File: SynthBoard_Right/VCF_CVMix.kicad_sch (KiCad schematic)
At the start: 21 parts, among them IC1 AS321KTR-G1, Q3 2SA812, Q4 2SC1623(RANGE:300-400), Q7 2SA812

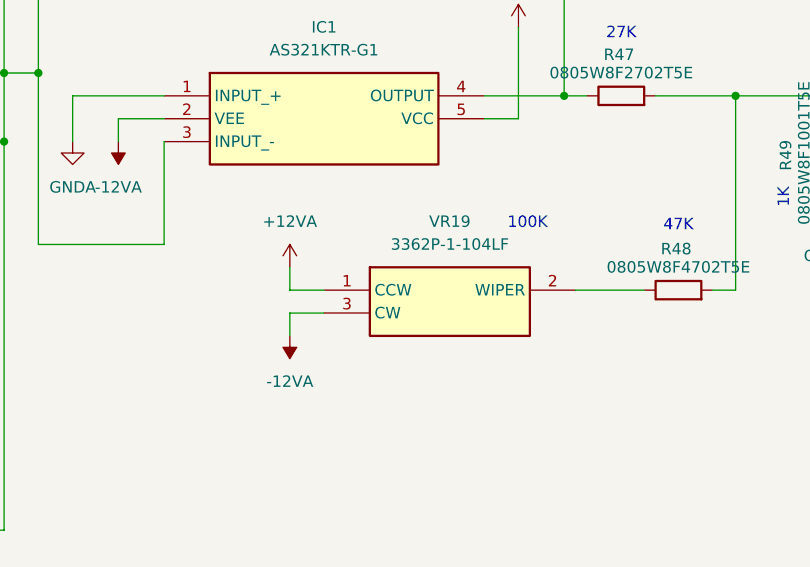
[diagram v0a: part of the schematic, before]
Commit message: SynthBoard Right
配線ミスを修正
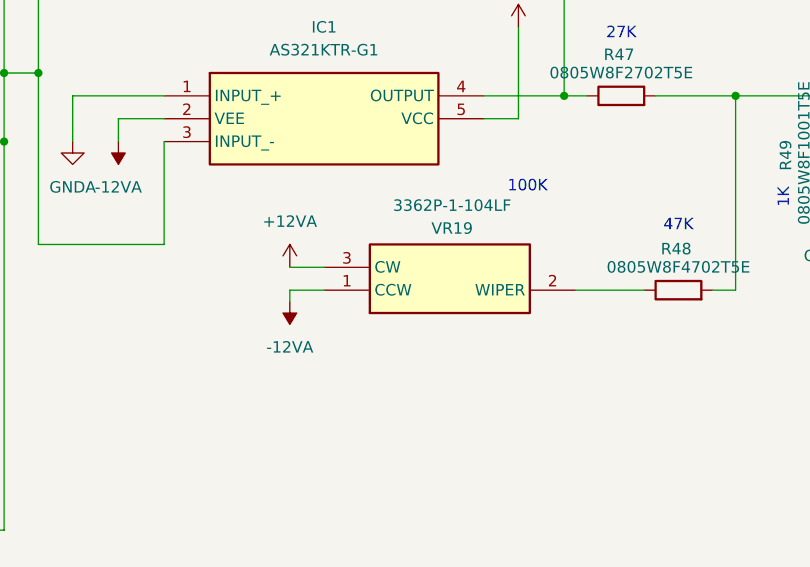
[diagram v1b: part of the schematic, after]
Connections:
- net +12VA: now also VR19.3 (CW); no longer VR19.1 (CCW)
- net -12VA: now also VR19.1 (CCW); no longer VR19.3 (CW)
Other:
- moved on the sheet: VR19
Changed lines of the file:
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@@
 	(text "100K"
 		(exclude_from_sim no)
-		(at 176.276 98.044 0)
+		(at 176.276 93.98 0)
 		(effects
 			(font
@@
 	(wire
 		(pts
-			(xy 153.67 105.41) (xy 149.86 105.41)
-		)
-		(stroke
-			(width 0)
-			(type default)
-		)
-	)
-	(wire
-		(pts
 			(xy 226.06 99.06) (xy 226.06 104.14)
 		)
@@
 	(wire
 		(pts
-			(xy 149.86 105.41) (xy 149.86 102.87)
+			(xy 66.04 121.92) (xy 68.58 121.92)
 		)
 		(stroke
@@
 	(wire
 		(pts
-			(xy 66.04 121.92) (xy 68.58 121.92)
+			(xy 81.28 16.51) (xy 81.28 20.32)
 		)
 		(stroke
@@
 	(wire
 		(pts
-			(xy 81.28 16.51) (xy 81.28 20.32)
+			(xy 85.09 140.97) (xy 85.09 147.32)
 		)
 		(stroke
@@
 	(wire
 		(pts
-			(xy 85.09 140.97) (xy 85.09 147.32)
+			(xy 121.92 100.33) (xy 121.92 81.28)
 		)
 		(stroke
@@
 	(wire
 		(pts
-			(xy 121.92 100.33) (xy 121.92 81.28)
+			(xy 135.89 83.82) (xy 125.73 83.82)
 		)
 		(stroke
@@
 	(wire
 		(pts
-			(xy 135.89 83.82) (xy 125.73 83.82)
+			(xy 149.86 102.87) (xy 153.67 102.87)
 		)
 		(stroke
@@
 	(wire
 		(pts
-			(xy 149.86 107.95) (xy 149.86 110.49)
-		)
-		(stroke
-			(width 0)
-			(type default)
-		)
-	)
-	(wire
-		(pts
 			(xy 125.73 83.82) (xy 125.73 88.9)
 		)
@@
 	(wire
 		(pts
-			(xy 153.67 107.95) (xy 149.86 107.95)
+			(xy 31.75 16.51) (xy 39.37 16.51)
 		)
 		(stroke
@@
 	(wire
 		(pts
-			(xy 31.75 16.51) (xy 39.37 16.51)
+			(xy 240.03 99.06) (xy 240.03 91.44)
 		)
 		(stroke
@@
 	(wire
 		(pts
-			(xy 240.03 99.06) (xy 240.03 91.44)
+			(xy 66.04 160.02) (xy 66.04 162.56)
 		)
 		(stroke
@@
 	(wire
 		(pts
-			(xy 66.04 160.02) (xy 66.04 162.56)
+			(xy 80.01 67.31) (xy 82.55 67.31)
 		)
 		(stroke
@@
 	(wire
 		(pts
-			(xy 80.01 67.31) (xy 82.55 67.31)
+			(xy 68.58 160.02) (xy 68.58 158.75)
 		)
 		(stroke
@@
 	(wire
 		(pts
-			(xy 68.58 160.02) (xy 68.58 158.75)
+			(xy 149.86 105.41) (xy 149.86 106.68)
 		)
 		(stroke
@@
 	(wire
 		(pts
+			(xy 153.67 105.41) (xy 149.86 105.41)
+		)
+		(stroke
+			(width 0)
+			(type default)
+		)
+	)
+	(wire
+		(pts
 			(xy 135.89 88.9) (xy 135.89 100.33)
 		)
@@
 	(symbol
 		(lib_id "power:-12VA")
-		(at 149.86 110.49 180)
+		(at 149.86 106.68 180)
 		(unit 1)
 		(exclude_from_sim no)
@@
 		(fields_autoplaced yes)
 		(property "Reference" "#PWR049"
-			(at 149.86 106.68 0)
+			(at 149.86 102.87 0)
 			(effects
 				(font
@@
 		)
 		(property "Value" "-12VA"
-			(at 149.86 115.57 0)
+			(at 149.86 111.76 0)
 			(effects
 				(font
@@
 		)
 		(property "Footprint" ""
-			(at 149.86 110.49 0)
+			(at 149.86 106.68 0)
 			(effects
 				(font
@@
 		)
 		(property "Datasheet" ""
-			(at 149.86 110.49 0)
+			(at 149.86 106.68 0)
 			(effects
 				(font
@@
 		)
 		(property "Description" "Power symbol creates a global label with name \"-12VA\""
-			(at 149.86 110.49 0)
+			(at 149.86 106.68 0)
 			(effects
 				(font
@@
 		(lib_id "SamacSys_Parts:3362P-1-103LF")
 		(at 153.67 105.41 0)
+		(mirror x)
 		(unit 1)
 		(exclude_from_sim no)
@@
 		(on_board yes)
 		(dnp no)
-		(fields_autoplaced yes)
 		(property "Reference" "VR19"
-			(at 167.64 97.79 0)
+			(at 167.894 98.552 0)
 			(effects
 				(font
@@
 		)
 		(property "Value" "3362P-1-104LF"
-			(at 167.64 100.33 0)
+			(at 167.894 96.012 0)
 			(effects
 				(font
@@
 		)
 		(property "Footprint" "SamacSys_parts:3362P_1"
-			(at 177.8 200.33 0)
+			(at 177.8 10.49 0)
 			(effects
 				(font
@@
 		)
 		(property "Datasheet" "https://datasheet.datasheetarchive.com/originals/distributors/SFDatasheet-6/sf-000139931.pdf"
-			(at 177.8 300.33 0)
+			(at 177.8 -89.51 0)
 			(effects
 				(font
@@
 		)
 		(property "Height" ""
-			(at 177.8 500.33 0)
+			(at 177.8 -289.51 0)
 			(effects
 				(font
@@
 		)
 		(property "Manufacturer_Name" "Bourns"
-			(at 177.8 600.33 0)
+			(at 177.8 -389.51 0)
 			(effects
 				(font
@@
 		)
 		(property "Manufacturer_Part_Number" "3362P-1-103LF"
-			(at 177.8 700.33 0)
+			(at 177.8 -489.51 0)
 			(effects
 				(font
@@
 		)
 		(property "Mouser Part Number" "652-3362P-1-103LF"
-			(at 177.8 800.33 0)
+			(at 177.8 -589.51 0)
 			(effects
 				(font
@@
 		)
 		(property "Mouser Price/Stock" "https://www.mouser.co.uk/ProductDetail/Bourns/3362P-1-103LF?qs=tS7CBNq%252BQ07BavGNEQud%252BA%3D%3D"
-			(at 177.8 900.33 0)
+			(at 177.8 -689.51 0)
 			(effects
 				(font
@@
 		)
 		(property "Arrow Part Number" "3362P-1-103LF"
-			(at 177.8 1000.33 0)
+			(at 177.8 -789.51 0)
 			(effects
 				(font
@@
 		)
 		(property "Arrow Price/Stock" "https://www.arrow.com/en/products/3362p-1-103lf/bourns?utm_currency=USD&region=nac"
-			(at 177.8 1100.33 0)
+			(at 177.8 -889.51 0)
 			(effects
 				(font

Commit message: SynthBoard Right
Basic部品で更新まで
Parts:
- removed Q4: 2SC1623(RANGE:300-400), SamacSys_parts:SOT95P237X125-3N, symbol SamacSys_Parts:2SC1623-A
- added Q1: SS8050(RANGE:200-350), Package_TO_SOT_SMD:SOT-23, symbol Transistor_BJT:SS8050
- R50: value 0805W8J0104T5E -> 0805W8F1003T5E
- renumbered Q3 to Q4
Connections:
- net +12VA: now also Q1.3 (C)
- net at R47.2, R48.2, R49.2: now also Q1.1 (B)
- net at Q4.1 (B), R50.2: now also Q1.2 (E)
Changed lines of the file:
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@@
 	(wire
 		(pts
-			(xy 226.06 91.44) (xy 226.06 99.06)
-		)
-		(stroke
-			(width 0)
-			(type default)
-		)
-	)
-	(wire
-		(pts
-			(xy 209.55 83.82) (xy 215.9 83.82)
+			(xy 209.55 83.82) (xy 218.44 83.82)
 		)
 		(stroke
@@
 	(wire
 		(pts
+			(xy 226.06 76.2) (xy 226.06 78.74)
+		)
+		(stroke
+			(width 0)
+			(type default)
+		)
+	)
+	(wire
+		(pts
 			(xy 196.85 105.41) (xy 199.39 105.41)
 		)
@@
 	(wire
 		(pts
+			(xy 226.06 88.9) (xy 226.06 99.06)
+		)
+		(stroke
+			(width 0)
+			(type default)
+		)
+	)
+	(wire
+		(pts
 			(xy 31.75 16.51) (xy 39.37 16.51)
 		)
@@
 		(on_board yes)
 		(dnp no)
-		(property "Reference" "Q3"
+		(property "Reference" "Q4"
 			(at 261.62 90.1699 0)
 			(effects
@@
 			(project "SynthBoard"
 				(path "/92765e2f-a998-485f-b610-76a9d5b50cba/91d0d04c-ea81-4181-b7cc-4c199a791c3e"
-					(reference "Q3")
+					(reference "Q4")
 					(unit 1)
 				)
@@
 			)
 		)
-		(property "Value" "0805W8J0104T5E"
+		(property "Value" "0805W8F1003T5E"
 			(at 223.52 107.95 90)
 			(effects
@@
 	)
 	(symbol
+		(lib_id "Transistor_BJT:SS8050")
+		(at 223.52 83.82 0)
+		(unit 1)
+		(exclude_from_sim no)
+		(in_bom yes)
+		(on_board yes)
+		(dnp no)
+		(fields_autoplaced yes)
+		(property "Reference" "Q1"
+			(at 228.6 82.5499 0)
+			(effects
+				(font
+					(size 1.27 1.27)
+				)
+				(justify left)
+			)
+		)
+		(property "Value" "SS8050(RANGE:200-350)"
+			(at 228.6 85.0899 0)
+			(effects
+				(font
+					(size 1.27 1.27)
+				)
+				(justify left)
+			)
+		)
+		(property "Footprint" "Package_TO_SOT_SMD:SOT-23"
+			(at 228.6 91.186 0)
+			(effects
+				(font
+					(size 1.27 1.27)
+					(italic yes)
+				)
+				(justify left)
+				(hide yes)
+			)
+		)
+		(property "Datasheet" "http://www.secosgmbh.com/datasheet/products/SSMPTransistor/SOT-23/SS8050.pdf"
+			(at 228.6 88.646 0)
+			(effects
+				(font
+					(size 1.27 1.27)
+				)
+				(justify left)
+				(hide yes)
+			)
+		)
+		(property "Description" "General Purpose NPN Transistor, 1.5A Ic, 25V Vce, SOT-23"
+			(at 257.556 86.106 0)
+			(effects
+				(font
+					(size 1.27 1.27)
+				)
+				(hide yes)
+			)
+		)
+		(pin "2"
+		)
+		(pin "3"
+		)
+		(pin "1"
+		)
+		(instances
+			(project ""
+				(path "/92765e2f-a998-485f-b610-76a9d5b50cba/91d0d04c-ea81-4181-b7cc-4c199a791c3e"
+					(reference "Q1")
+					(unit 1)
+				)
+			)
+		)
+	)
+	(symbol
 		(lib_id "SamacSys_Parts:AS321KTR-E1")
 		(at 135.89 83.82 0)
@@
 					(unit 1)
 				)
-			)
-		)
-	)
-	(symbol
-		(lib_id "SamacSys_Parts:2SC1623-A")
-		(at 215.9 83.82 0)
-		(unit 1)
-		(exclude_from_sim no)
-		(in_bom yes)
-		(on_board yes)
-		(dnp no)
-		(fields_autoplaced yes)
-		(property "Reference" "Q4"
-			(at 229.87 82.5499 0)
-			(effects
-				(font
-					(size 1.27 1.27)
-				)
-				(justify left)
-			)
-		)
-		(property "Value" "2SC1623(RANGE:300-400)"
-			(at 229.87 85.0899 0)
-			(effects
-				(font
-					(size 1.27 1.27)
-				)
-				(justify left)
-			)
-		)
-		(property "Footprint" "SamacSys_parts:SOT95P237X125-3N"
-			(at 229.87 185.09 0)
-			(effects
-				(font
-					(size 1.27 1.27)
-				)
-				(justify left top)
-				(hide yes)
-			)
-		)
-		(property "Datasheet" "https://www.mouser.in/datasheet/2/258/2SC1623_SOT_23_-1625845.pdf"
-			(at 229.87 285.09 0)
-			(effects
-				(font
-					(size 1.27 1.27)
-				)
-				(justify left top)
-				(hide yes)
-			)
-		)
-		(property "Description" "Renesas Electronics 2SC1623-A NPN Bipolar Transistor, 100 mA, 50 V, 3-Pin MiniMold"
-			(at 215.9 83.82 0)
-			(effects
-				(font
-					(size 1.27 1.27)
-				)
-				(hide yes)
-			)
-		)
-		(property "Height" "1.25"
-			(at 229.87 485.09 0)
-			(effects
-				(font
-					(size 1.27 1.27)
-				)
-				(justify left top)
-				(hide yes)
-			)
-		)
-		(property "Manufacturer_Name" "Renesas Electronics"
-			(at 229.87 585.09 0)
-			(effects
-				(font
-					(size 1.27 1.27)
-				)
-				(justify left top)
-				(hide yes)
-			)
-		)
-		(property "Manufacturer_Part_Number" "2SC1623-A"
-			(at 229.87 685.09 0)
-			(effects
-				(font
-					(size 1.27 1.27)
-				)
-				(justify left top)
-				(hide yes)
-			)
-		)
-		(property "Mouser Part Number" ""
-			(at 229.87 785.09 0)
-			(effects
-				(font
-					(size 1.27 1.27)
-				)
-				(justify left top)
-				(hide yes)
-			)
-		)
-		(property "Mouser Price/Stock" ""
-			(at 229.87 885.09 0)
-			(effects
-				(font
-					(size 1.27 1.27)
-				)
-				(justify left top)
-				(hide yes)
-			)
-		)
-		(property "Arrow Part Number" ""
-			(at 229.87 985.09 0)
-			(effects
-				(font
-					(size 1.27 1.27)
-				)
-				(justify left top)
-				(hide yes)
-			)
-		)
-		(property "Arrow Price/Stock" ""
-			(at 229.87 1085.09 0)
-			(effects
-				(font
-					(size 1.27 1.27)
-				)
-				(justify left top)
-				(hide yes)
-			)
-		)
-		(pin "3"
-		)
-		(pin "2"
-		)
-		(pin "1"
-		)
-		(instances
-			(project "SynthBoard"
-				(path "/92765e2f-a998-485f-b610-76a9d5b50cba/91d0d04c-ea81-4181-b7cc-4c199a791c3e"
-					(reference "Q4")
-					(unit 1)
-				)

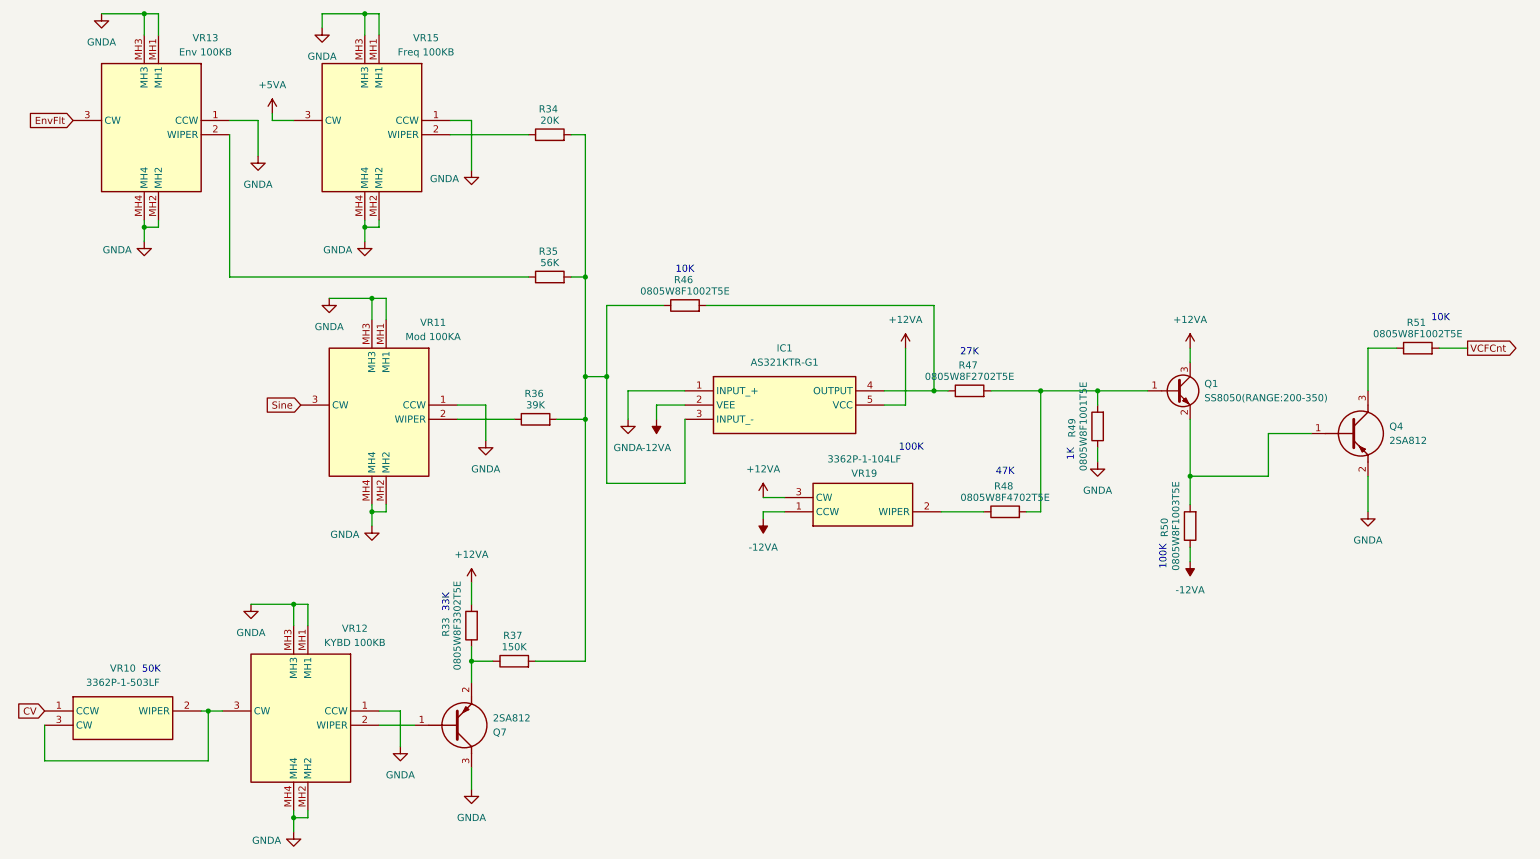
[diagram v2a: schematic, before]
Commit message: MC2
まとめて登録
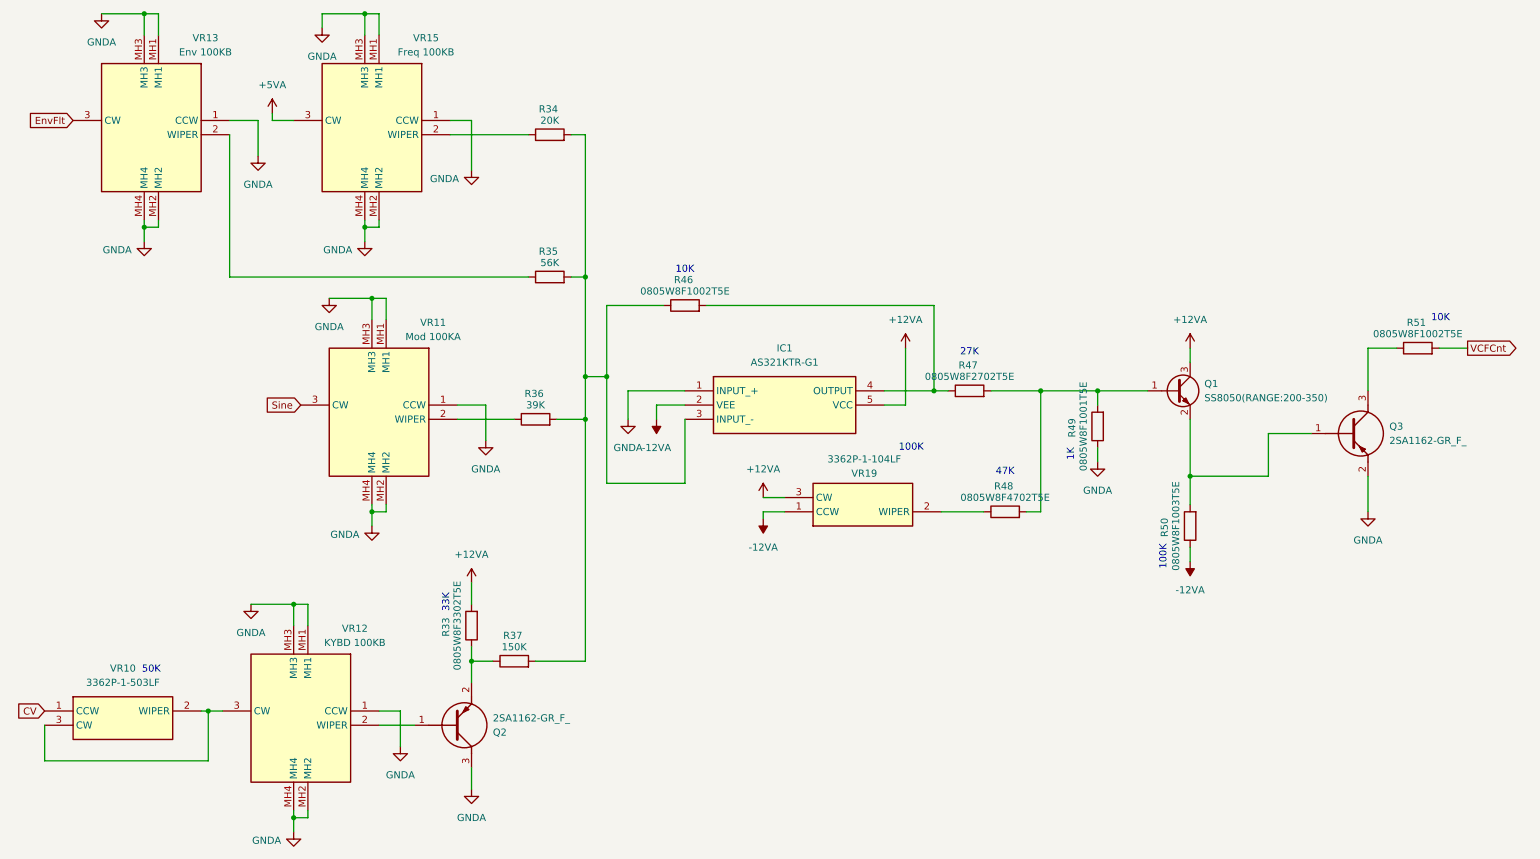
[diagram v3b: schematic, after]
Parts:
- removed Q4, Q7: 2SA812, SamacSys_parts:SOT95P240X120-3N, symbol SamacSys_Parts:2SA812
- added Q2, Q3: 2SA1162-GR_F_, SamacSys_parts:1SS294LFT, symbol SamacSys_Parts:2SA1162-GR_F_
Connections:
- net GNDA: now also Q2.3 (C), Q3.2 (E)
- net at VR12.2 (WIPER): now also Q2.1 (B)
- net at R33.1, R37.1: now also Q2.2 (E)
- net at Q1.2 (E), R50.2: now also Q3.1 (B)
- net at R51.1: now also Q3.3 (C)
